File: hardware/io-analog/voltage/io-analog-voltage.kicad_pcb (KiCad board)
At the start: 2 copper layers, 60 x 60 mm, 28 parts, among them J1 Analog Extension, J2 Output, J3 Power, J4 Power, U1 TLV2772, U2 TLV2772, U3 LM317T

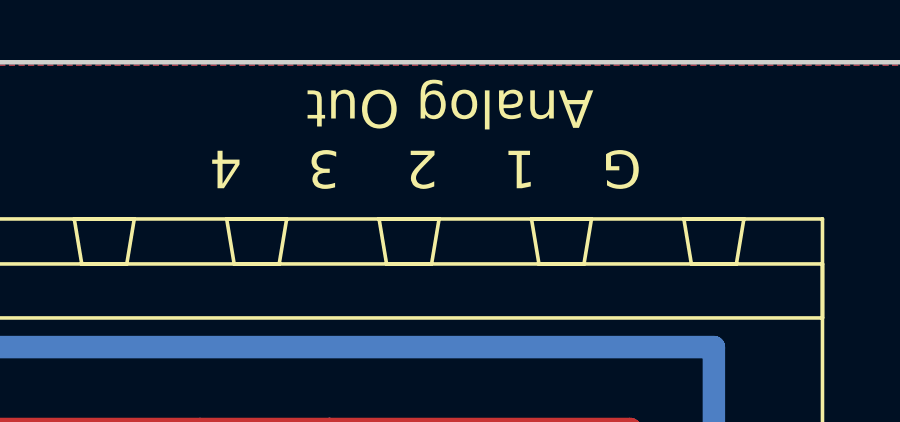
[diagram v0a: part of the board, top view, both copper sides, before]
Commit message: Finalize PWM and Voltage modules (1 each).
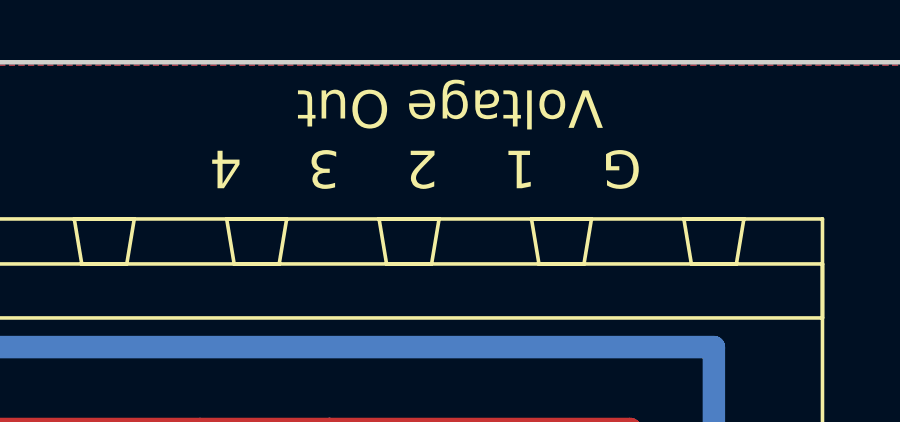
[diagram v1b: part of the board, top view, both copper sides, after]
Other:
- board text added: "G 1 2 3 4 Voltage Out"
- board text removed: "G 1 2 3 4 Analog Out"
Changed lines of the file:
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@@
   (page A4)
   (title_block
-    (title "DMX Demonstrator - Analog IO Amplify (DMX-IO3)")
+    (title "DMX Demonstrator - Analog IO Voltage (DMX-IO3)")
     (date 2023-07-01)
     (rev 1.2)
@@
   )
   (layers
-    (0 F.Cu signal)
-    (31 B.Cu signal)
+    (0 F.Cu signal hide)
+    (31 B.Cu signal hide)
     (32 B.Adhes user)
     (33 F.Adhes user)
@@
     (38 B.Mask user)
     (39 F.Mask user)
-    (40 Dwgs.User user)
+    (40 Dwgs.User user hide)
     (41 Cmts.User user)
     (42 Eco1.User user)
@@
     (44 Edge.Cuts user)
     (45 Margin user)
-    (46 B.CrtYd user)
-    (47 F.CrtYd user)
-    (48 B.Fab user)
-    (49 F.Fab user)
+    (46 B.CrtYd user hide)
+    (47 F.CrtYd user hide)
+    (48 B.Fab user hide)
+    (49 F.Fab user hide)
   )
   (setup
@@
     (effects (font (size 1.5 1.5) (thickness 0.3)))
   )
-  (gr_text "   G    1    2    3    4\nAnalog Out" (at 165.0619 76.3397 180) (layer F.SilkS)
+  (gr_text "   G    1    2    3    4\nVoltage Out" (at 165.0619 76.3397 180) (layer F.SilkS)
     (effects (font (size 1.25 1.25) (thickness 0.25)))
   )

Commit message: Finalize io-analog boards.
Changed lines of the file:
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@@
     (pcbplotparams
       (layerselection 0x010fc_ffffffff)
-      (usegerberextensions false)
+      (usegerberextensions true)
       (usegerberattributes false)
       (usegerberadvancedattributes false)
@@
       (psa4output false)
       (plotreference true)
-      (plotvalue true)
+      (plotvalue false)
       (plotinvisibletext false)
       (padsonsilk false)
-      (subtractmaskfromsilk false)
+      (subtractmaskfromsilk true)
       (outputformat 1)
       (mirror false)
-      (drillshape 1)
+      (drillshape 0)
       (scaleselection 1)
-      (outputdirectory ""))
+      (outputdirectory "grb"))
   )
   (net 0 "")
@@
       (xy -1.404739 2.654895) (xy -1.386268 2.656083) (xy -1.36631 2.655905)) (layer B.SilkS) (width 0.01))
   )
+  (gr_arc (start 185.57748 133.0325) (end 185.53178 133.7945) (angle -90) (layer Edge.Cuts) (width 0.15))
   (gr_line (start 411.226 134.8105) (end 411.1625 134.874) (layer Dwgs.User) (width 0.15))
   (gr_text "Analog Extention" (at 184.785 102.8065 90) (layer F.SilkS)
@@
   )
   (gr_line (start 127.0914 73.8175) (end 185.5114 73.8175) (layer Edge.Cuts) (width 0.15))
-  (gr_line (start 186.3472 74.6355) (end 186.342 132.969) (layer Edge.Cuts) (width 0.15))
-  (gr_arc (start 185.5292 133.0325) (end 185.4835 133.7945) (angle -90) (layer Edge.Cuts) (width 0.15))
+  (gr_line (start 186.3472 74.5795) (end 186.342 133.0555) (layer Edge.Cuts) (width 0.15))
   (gr_arc (start 185.5292 74.6355) (end 186.3472 74.6355) (angle -90) (layer Edge.Cuts) (width 0.15))
   (gr_arc (start 127.0914 74.5795) (end 127.0914 73.8175) (angle -90) (layer Edge.Cuts) (width 0.15))
   (gr_arc (start 127.0965 133.0325) (end 126.3345 133.0325) (angle -90) (layer Edge.Cuts) (width 0.15))
-  (gr_line (start 127.0965 133.7945) (end 185.4835 133.7945) (layer Edge.Cuts) (width 0.15))
+  (gr_line (start 127.0914 133.7945) (end 185.5114 133.7945) (layer Edge.Cuts) (width 0.15))
   (gr_line (start 126.3294 133.0555) (end 126.3294 74.5795) (layer Edge.Cuts) (width 0.15))
   (gr_text "DMX-IO3, Rev 1.2\nCrazy Giraffe Software\n\n" (at 147.6375 129.9845) (layer B.SilkS)

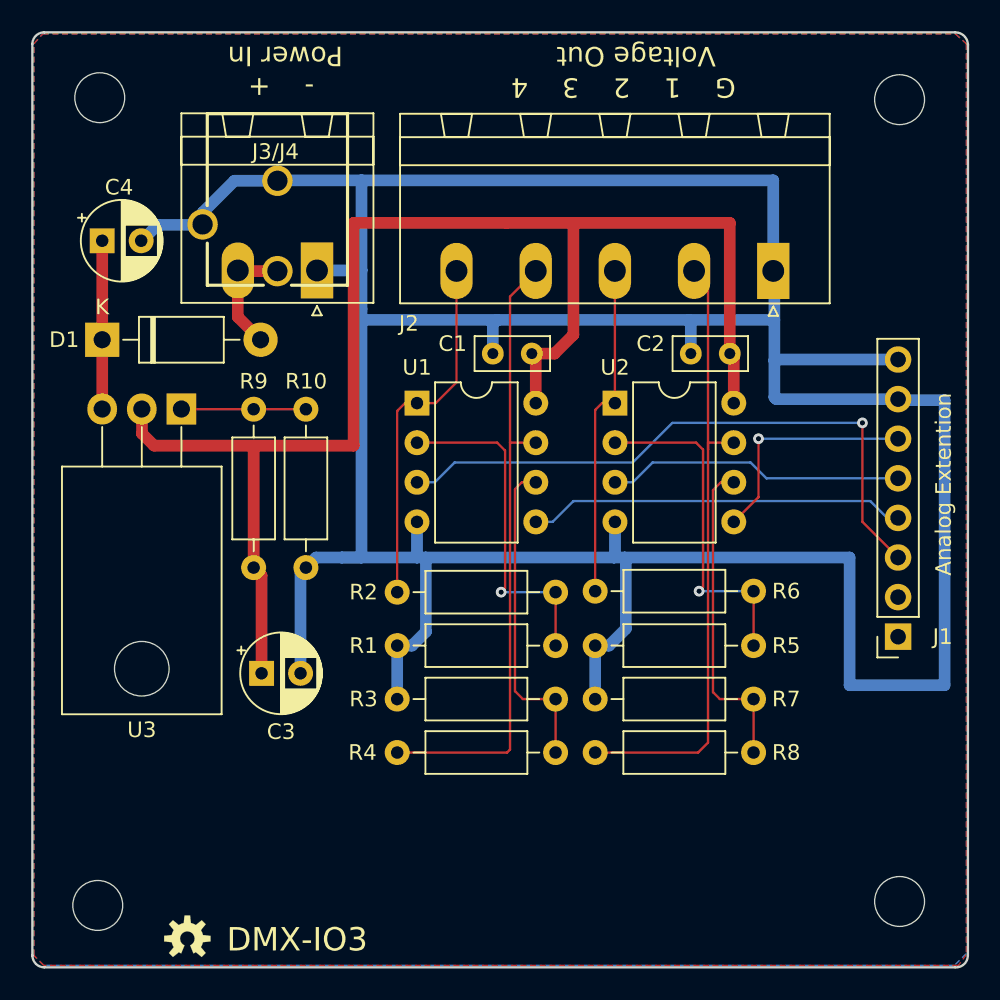
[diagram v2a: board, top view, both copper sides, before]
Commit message: Display Pro: - Switch to smaller screw terminal connectors - Add pull-down resistors - Add silkscreen values - Remove COAX power connector...again - Add test software
Core:
- Fix issue with A03 and A02 being reversed at Analog Extensions
- Fix issue with A1 and A0 at IO Extension header
- Label D0..D7 correctly
- Swap U4 and U5 in schematic to match board layout
- Change TO-92 footprint
- Add silkscreen values
- Add test software

PWM:
- Switch to smaller screw terminal connectors
- Add silkscreen values
- Remove COAX power connector

Voltage:
- Switch to smaller screw terminal connectors
- Add silkscreen values
- Remove COAX power connector

DMX:
- Fix issue with DMX A and B being reversed
- Group bypass-only resistors together
- Add ISO bypass solder bridges
- Add silkscreen values
- Remove RDM bias resistors
- Add test software

Rx-IO:
- Fix issue with A1 and A0 at IO Extension header
- Add silkscreen values

Tx-IO:
- Switch to 74LS07 for Led driver
- Add pulldown resistor for discovery
- Add silkscreen values

Discovery:
- Make use of new Tx-IO pulldown resistor
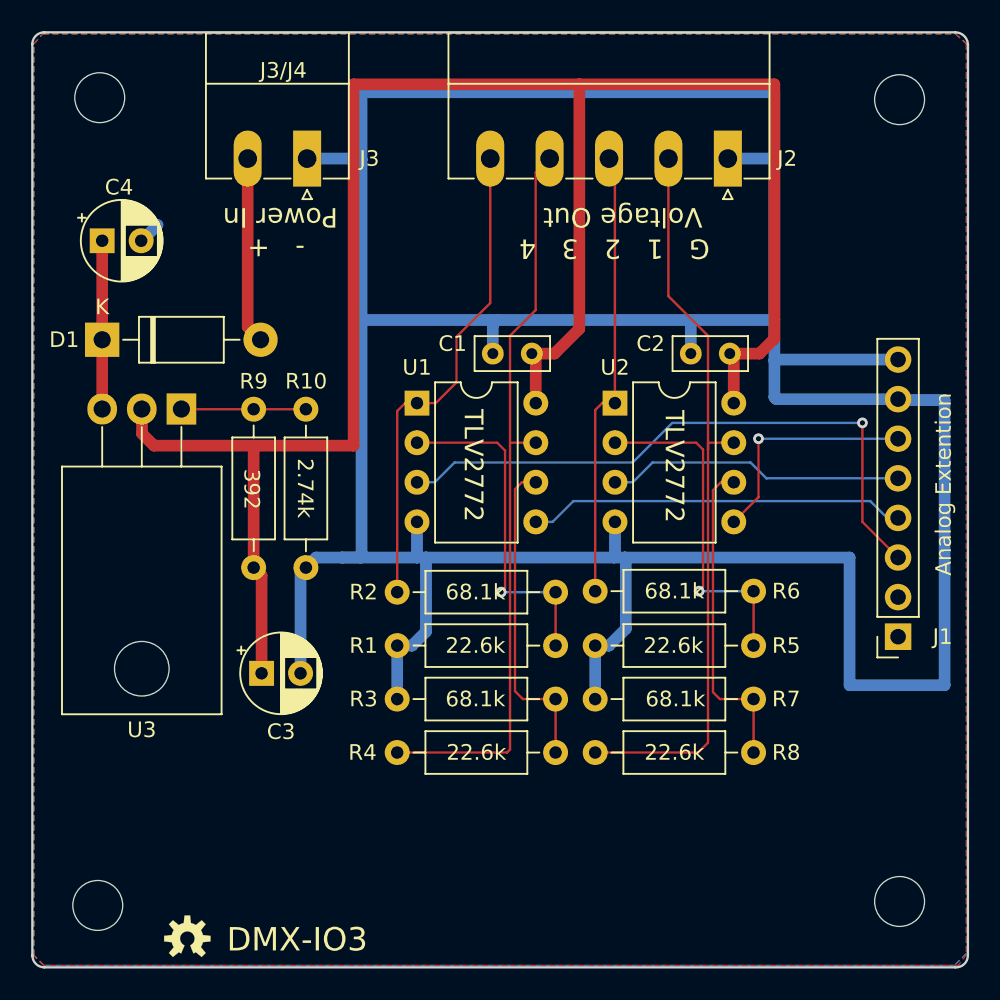
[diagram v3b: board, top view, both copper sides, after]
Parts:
- removed J4: Power, Connectors:POWER_JACK_PTH_BREAD
- J2: footprint Connector_Phoenix_MSTB:PhoenixContact_MSTBA_2,5_5-G-5,08_1x05_P5.08mm_Horizontal -> Connector_Phoenix_MC:PhoenixContact_MC_1,5_5-G-3.81_1x05_P3.81mm_Horizontal
- J3: footprint Connector_Phoenix_MSTB:PhoenixContact_MSTBA_2,5_2-G-5,08_1x02_P5.08mm_Horizontal -> Connector_Phoenix_MC:PhoenixContact_MC_1,5_2-G-3.81_1x02_P3.81mm_Horizontal
- moved J2 7.77 mm to (170.9, 81.9)
- moved J3 7.20 mm to (144.0, 81.9)
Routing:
- net Net-(C1-Pad1): track 94.3 -> 126.3 mm
- net Net-(J2-Pad5): track 23.5 -> 31.6 mm
- net Net-(J2-Pad2): track 40.2 -> 48.1 mm
- net Net-(J2-Pad4): track 40.4 -> 47.9 mm
- net Net-(J2-Pad3): track 21.6 -> 28.9 mm
- net Net-(D1-Pad2): track 7.61 -> 12.0 mm
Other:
- board text added: "2.74k"
- board text added: "22.6k"
- board text added: "392"
- board text added: "68.1k"
- board text added: "DMX-IO3, Rev 1.3 Crazy Giraffe Software"
- board text added: "TLV2772"
- board text removed: "DMX-IO3, Rev 1.2 Crazy Giraffe Software"
